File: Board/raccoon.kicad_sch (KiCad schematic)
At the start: 57 parts, among them J1 USB_B, J2 Conn_01x03, J3 Conn_01x02, J4 Conn_01x03, J5 Conn_01x02, J6 Conn_02x08_Top_Bottom, J7 Conn_01x03, J8 Conn_01x02, J9 Conn_01x06, Q1 Q_NMOS_GSD, SW1 SW_SPST, SW2 SW_SPST, U1 TJA1027T, U2 TJA1027T, U3 AMS1117-5.0, U4 AMS1117-3.3, U5 NCV7356, U6 STM32F413RGTx, U7 TJA1042T-3, U8 TJA1042T-3, U9 TJA1042T-3, Y1 16MHz

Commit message: Added new STM32 and prepped schematic for wiring
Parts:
- removed U6: STM32F413RGTx, Package_QFP:LQFP-64_10x10mm_P0.5mm, symbol MCU_ST_STM32F4:STM32F413RGTx
- added C22, C24: 10p, Capacitor_SMD:C_0402_1005Metric, symbol Device:C
- added C23: 100n, Capacitor_SMD:C_0603_1608Metric, symbol Device:C
- added C25: 4.7u, Capacitor_SMD:C_0603_1608Metric, symbol Device:C
- added D5: LED_RGB, LED_SMD:LED_RGB_5050-6, symbol raccoon:LED_RGB
- added Q2: Q_NMOS_GSD, Package_TO_SOT_SMD:SOT-23, symbol Device:Q_NMOS_GSD
- added R10: 10k, Resistor_SMD:R_0603_1608Metric, symbol Device:R
- added SW3, SW4: SW_SPST, Button_Switch_THT:SW_PUSH_6mm_H8mm, symbol Switch:SW_SPST
- added U10: STM32G473CETx, Package_QFP:LQFP-48_7x7mm_P0.5mm, symbol MCU_ST_STM32G4:STM32G473CETx
- added U12: STM32F413RGTx, Package_QFP:LQFP-64_10x10mm_P0.5mm, symbol MCU_ST_STM32F4:STM32F413RGTx
- added Y2: 16MHz, Crystal:Crystal_SMD_3225-4Pin_3.2x2.5mm, symbol Device:Crystal_GND24_Small
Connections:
- net +3V3: now also U10.21 (VDDA), U10.24 (VDD), U10.36 (VDD), U10.48 (VDD), U12.13 (VDDA), U12.19 (VDD), U12.32 (VDD), U12.48 (VDD), U12.64 (VDD)
- net BOOT: now also R10.2, SW4.2 (B), U12.60 (BOOT0)
- net CAN1_RX: now also U12.61 (PB8)
- net CAN1_TX: now also U12.62 (PB9)
- net CAN2_RX: now also U12.57 (PB5)
- net CAN2_TX: now also U12.58 (PB6)
- net CAN3_RX: now also U12.41 (PA8)
- net CAN3_TX: now also U12.50 (PA15)
- net GMLAN_MODE0: now also U12.36 (PB15)
- net GMLAN_MODE1: now also U12.35 (PB14)
- net GMLAN_RX: now also U12.33 (PB12), U12.55 (PB3)
- net GMLAN_TX: now also U12.34 (PB13), U12.56 (PB4)
- net GND: now also C22.2, C23.2, C24.2, C25.1, Q2.2 (S), R10.1, SW3.1 (A), U10.19 (VSSA), U10.23 (VSS), U10.35 (VSS), U10.47 (VSS), U12.12 (VSSA), U12.18 (VSS), U12.31 (VSS), U12.47 (VSS), U12.63 (VSS), Y2.2, Y2.4
- net IGNITION: now also Q2.1 (G)
- net K_LIN_EN: now also U12.59 (PB7)
- net K_LIN_RX: now also U12.54 (PD2)
- net K_LIN_TX: now also U12.53 (PC12)
- net LED_BLUE: now also U12.37 (PC6)
- net LED_GREEN: now also U12.38 (PC7)
- net LED_RED: now also U12.40 (PC9)
- net L_LIN_EN: now also U12.49 (PA14)
- net L_LIN_RX: now also U12.52 (PC11)
- net L_LIN_TX: now also U12.51 (PC10)
- net SWDIO: now also U12.46 (PA13)
- net USB_DN: now also U12.44 (PA11)
- net USB_DP: now also U12.45 (PA12)
- net at Q1.3 (D): now also U10.8 (PA0)
- net at C10.1, Y1.3: now also U10.3 (PC14)
- net at C12.1, Y1.1: now also U10.4 (PC15)
- net ~CAN1_EN~ renamed ~{CAN1_EN}
- net ~{CAN1_EN}: now also U12.9 (PC1)
- net ~CAN2_EN~ renamed ~{CAN2_EN}
- net ~{CAN2_EN}: now also U12.2 (PC13)
- net ~CAN3_EN~ renamed ~{CAN3_EN}
- net ~{CAN3_EN}: now also U12.14 (PA0)
- net ~RST~ renamed ~{RST}
- net ~{RST}: now also C23.1, SW3.2 (B), U12.7 (NRST)
- new net: C22.1, U12.5 (PH0), Y2.3
- new net: C24.1, U12.6 (PH1), Y2.1
- new net: Q2.3 (D), U12.15 (PA1)
- new net: C25.2, U12.30 (VCAP_1)
- no-connect marks 25 -> 26
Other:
- moved on the sheet: C13

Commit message: ADDED usb c and some other stuff
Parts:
- removed J1: USB_B, Connector_USB:USB_B_OST_USB-B1HSxx_Horizontal, symbol Connector:USB_B
- added D6, D7: D, Diode_SMD:D_0603_1608Metric, symbol Simulation_SPICE:D
- added J1: USB_C_Receptacle_USB2.0_14P, Connector_USB:USB_C_Receptacle_GCT_USB4105-xx-A_16P_TopMnt_Horizontal, symbol Connector:USB_C_Receptacle_USB2.0_14P
- added JP1, JP2: N/C, symbol Jumper:SolderJumper_2_Open
- added R11, R12: 5.1k, Resistor_SMD:R_01005_0402Metric, symbol Device:R
- added R13, R14: 1k, Resistor_SMD:R_0402_1005Metric, symbol Device:R
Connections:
- net +12V: now also D6.2 (A), D7.2 (A)
- net GND: now also J1.A1 (GND), J1.A12 (GND), J1.B1 (GND), J1.B12 (GND), J1.SH (SHIELD), JP1.1 (A), JP2.1 (A), R11.2, R12.1
- net K_LIN: no longer J3.1 (Pin_1)
- net K_LIN_EN: no longer U1.2 (~{SLP})
- net K_LIN_RX: no longer U1.1 (RXD)
- net K_LIN_TX: no longer U1.4 (TXD)
- net L_LIN: no longer J5.1 (Pin_1)
- net L_LIN_EN: no longer U2.2 (~{SLP})
- net L_LIN_RX: no longer U2.1 (RXD)
- net L_LIN_TX: no longer U2.4 (TXD)
- net USB_DN: now also R1.1; no longer R2.2
- net USB_DP: now also R2.2; no longer R1.1
- net at C12.1, Y1.1: no longer U10.4 (PC15)
- net at C10.1, Y1.3: no longer U10.3 (PC14)
- net at D1.2 (A): now also J1.A4 (VBUS), J1.A9 (VBUS), J1.B4 (VBUS), J1.B9 (VBUS)
- net at R2.1: now also J1.A6 (D+), J1.B6 (D+)
- net at R1.2: now also J1.A7 (D-), J1.B7 (D-)
- new net: J1.A5 (CC1), R11.1
- new net: J1.B5 (CC2), R12.2
- new net: JP2.2 (B), R13.2
- new net: D7.1 (K), R14.1
- new net: JP1.2 (B), R14.2
- new net: D6.1 (K), R13.1
- new net LIN1: J3.1 (Pin_1)
- new net LIN1_EN: U1.2 (~{SLP})
- new net LIN1_RX: U1.1 (RXD)
- new net LIN1_TX: U1.4 (TXD)
- new net LIN2: J5.1 (Pin_1)
- new net LIN2_EN: U2.2 (~{SLP})
- new net LIN2_RX: U2.1 (RXD)
- new net LIN2_TX: U2.4 (TXD)
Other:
- moved on the sheet: C1, C3, D1, D3, D4, Q1, R1, R2, R8, R9, U1

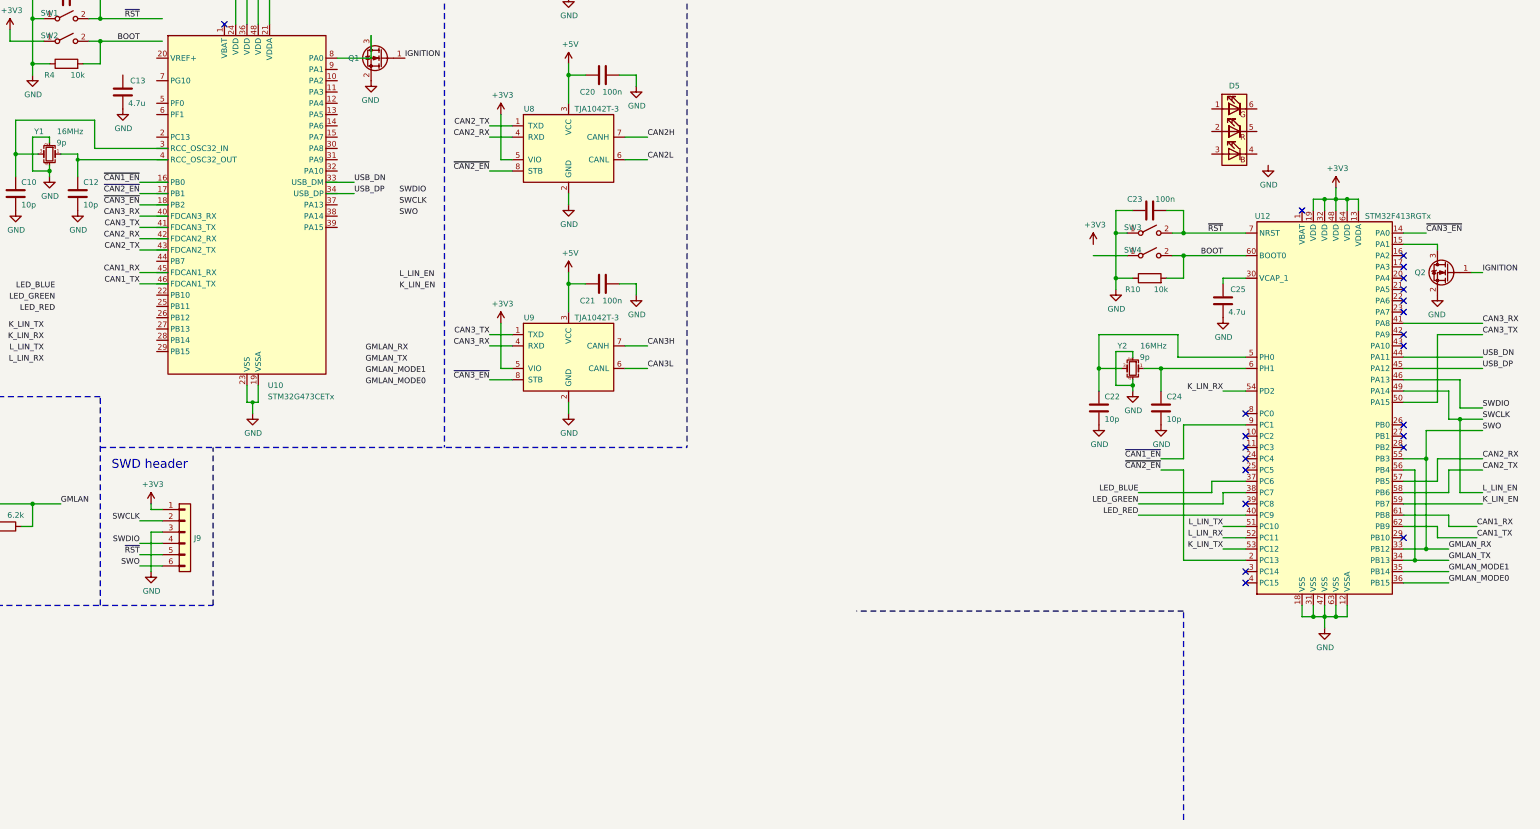
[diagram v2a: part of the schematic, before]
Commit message: deleted traces and added footprints
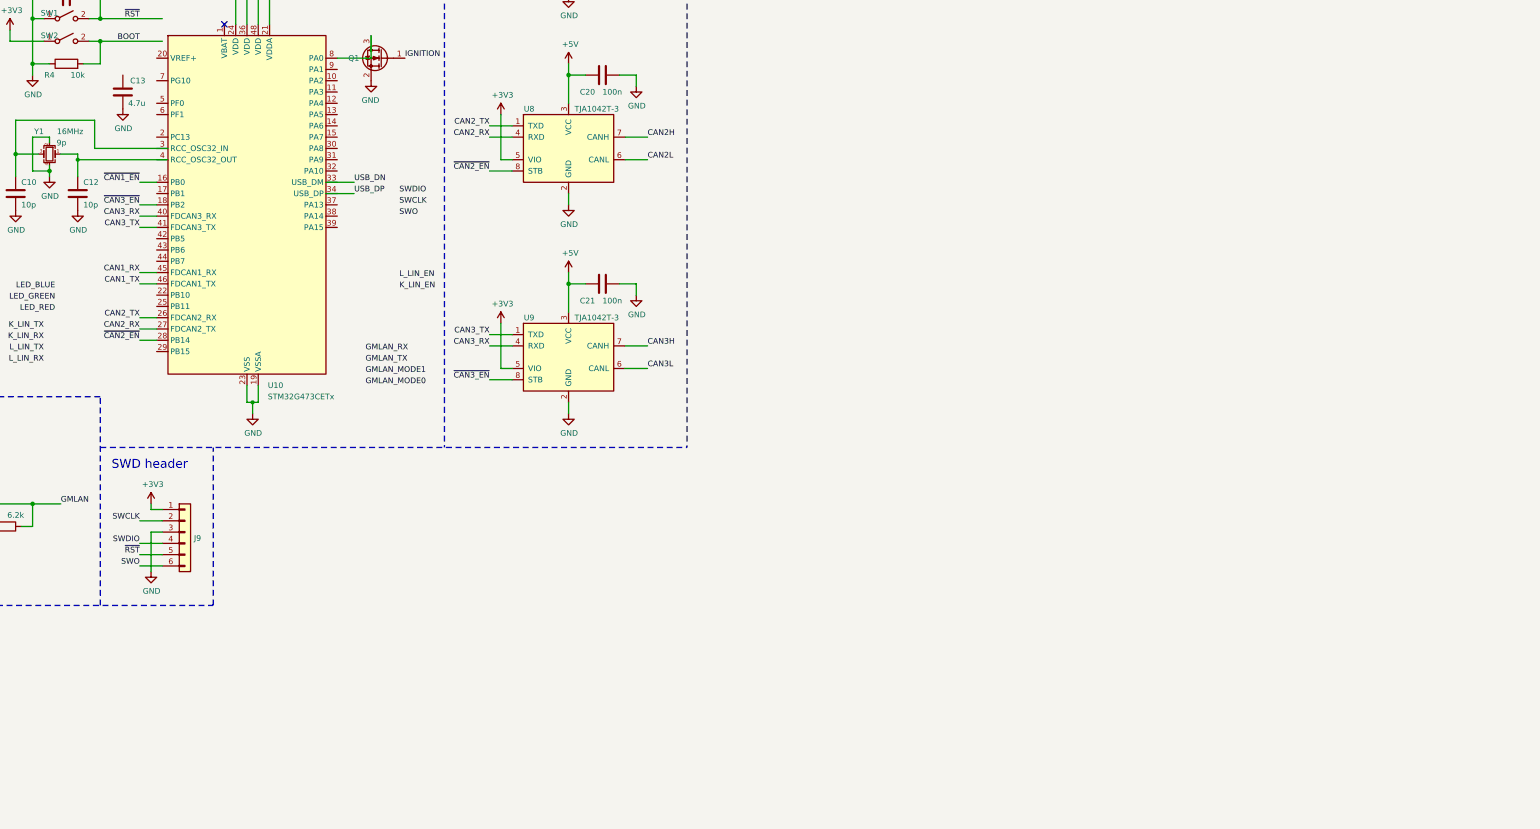
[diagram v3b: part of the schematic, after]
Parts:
- removed C22, C24: 10p, Capacitor_SMD:C_0402_1005Metric, symbol Device:C
- removed C23: 100n, Capacitor_SMD:C_0603_1608Metric, symbol Device:C
- removed C25: 4.7u, Capacitor_SMD:C_0603_1608Metric, symbol Device:C
- removed D5: LED_RGB, LED_SMD:LED_RGB_5050-6, symbol raccoon:LED_RGB
- removed Q2: Q_NMOS_GSD, Package_TO_SOT_SMD:SOT-23, symbol Device:Q_NMOS_GSD
- removed R10: 10k, Resistor_SMD:R_0603_1608Metric, symbol Device:R
- removed SW3, SW4: SW_SPST, Button_Switch_THT:SW_PUSH_6mm_H8mm, symbol Switch:SW_SPST
- removed U12: STM32F413RGTx, Package_QFP:LQFP-64_10x10mm_P0.5mm, symbol MCU_ST_STM32F4:STM32F413RGTx
- removed Y2: 16MHz, Crystal:Crystal_SMD_3225-4Pin_3.2x2.5mm, symbol Device:Crystal_GND24_Small
- JP1, JP2: footprint (none) -> Jumper:SolderJumper-2_P1.3mm_Open_RoundedPad1.0x1.5mm
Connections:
- net CAN1_RX: now also U10.45 (PB8)
- net CAN1_TX: now also U10.46 (PB9)
- net CAN2_RX: now also U10.27 (PB13)
- net CAN2_TX: now also U10.26 (PB12)
- net CAN3_RX: now also U10.40 (PB3)
- net CAN3_TX: now also U10.41 (PB4)
- net GMLAN_RX: no longer J9.6 (Pin_6)
- net L_LIN_EN: no longer J9.2 (Pin_2)
- net ~{CAN1_EN}: now also U10.16 (PB0)
- net ~{CAN2_EN}: now also U10.28 (PB14)
- net ~{CAN3_EN}: now also U10.18 (PB2)
- new net SWCLK: J9.2 (Pin_2)
- new net SWO: J9.6 (Pin_6)
- no-connect marks 26 -> 5

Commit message: uhh changed some more stuff idk
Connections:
- net ~{CAN1_EN}: no longer U10.16 (PB0)
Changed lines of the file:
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@@
-		)
-	)
-	(wire
-		(pts
-			(xy 154.94 97.79) (xy 158.75 97.79)
-		)
-		(stroke
-			(width 0)
-			(type default)
 		)
 	)
@@
 	)
 	(label "~{CAN1_EN}"
-		(at 154.94 97.79 180)
-		(effects
-			(font
+		(at 154.94 115.57 180)
+		(effects
+			(font
